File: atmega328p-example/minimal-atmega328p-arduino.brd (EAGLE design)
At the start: 67.3 x 33 mm, 19 parts, among them J1 3x2 M, J4 POWER_JACK, U1 NCP1117ST50T3G, U4 ATMEGA328P-PU, X1 CSTCE16M0V53-R0 16MHZ

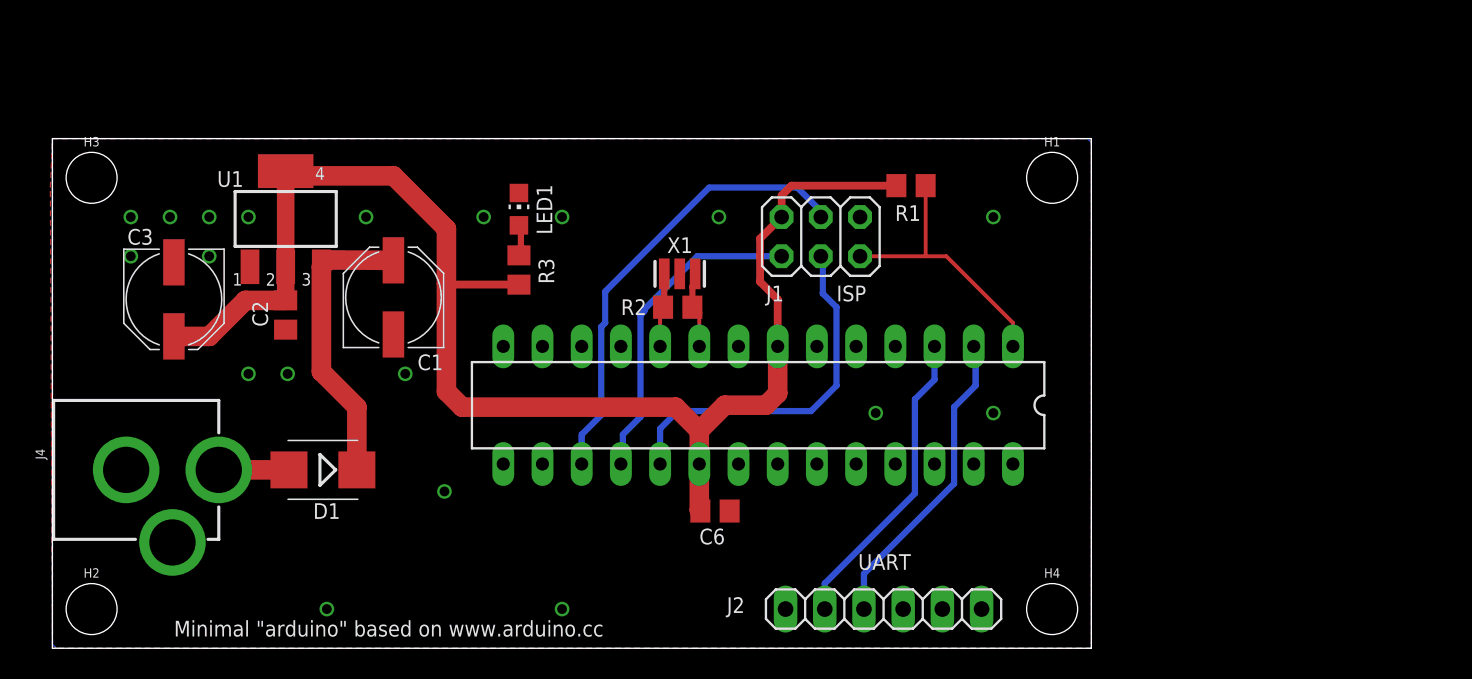
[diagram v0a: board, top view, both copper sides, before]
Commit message: Updated ATMEGA328P schematic and layout to modernish standards. Still needs attributes and BOM.
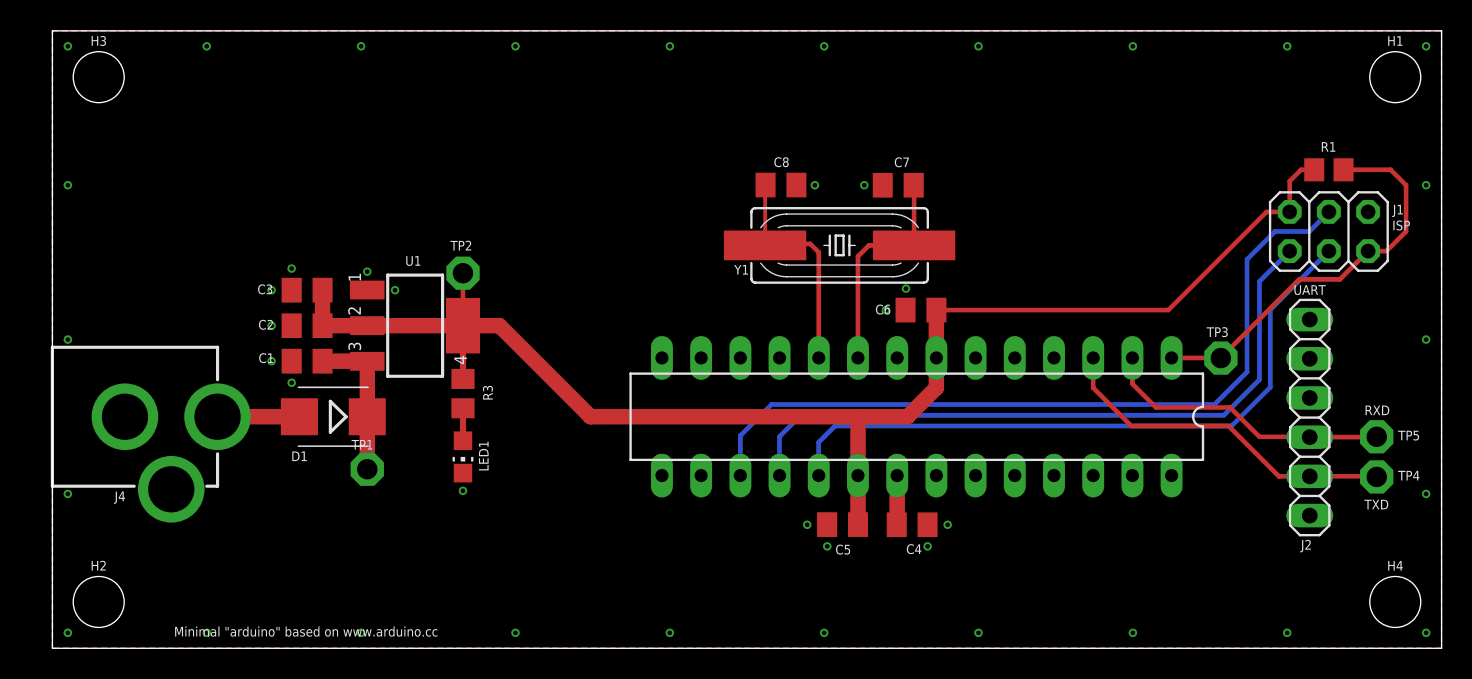
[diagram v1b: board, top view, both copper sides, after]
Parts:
- removed R2: 1M, rcl:R0805
- removed X1: CSTCE16M0V53-R0 16MHZ, SmartPrj:RESONATOR
- added C4, C5: 100n, rcl:C0805K
- added C7, C8: 18p, rcl:C0805K
- added TP1, TP2, TP3, TP4, TP5: TPPAD1-13, testpad:P1-13
- added Y1: 16 MHz, SparkFun-Clocks:HC49UP
- C1, C3: device rcl:PANASONIC_D -> rcl:C0805K
- C2, C6: device rcl:C0805 -> rcl:C0805K
- moved J1 32.9 mm to (82.7, 27.0)
- moved J2 30.3 mm to (81.5, 14.9), turned to 90 degrees
- moved R1 27.1 mm to (82.7, 31.0)
- moved H1 23.2 mm to (87.0, 37.0)
- moved H4 22.2 mm to (87.0, 3.00)
- moved C6 18.6 mm to (56.3, 21.9), turned to 0 degrees
- moved LED1 16.5 mm to (26.6, 12.4), turned to 180 degrees
- moved U1 10.9 mm to (23.5, 20.9), turned to 270 degrees
- moved U4 10.3 mm to (56.0, 15.0)
- moved R3 8.79 mm to (26.6, 16.5), turned to 90 degrees
- moved C3 8.65 mm to (16.5, 23.2), turned to 180 degrees
- moved C1 6.96 mm to (16.5, 18.6), turned to 180 degrees
- moved H3 6.54 mm to (3.00, 37.0)
- moved D1 3.51 mm to (18.2, 15.0)
- moved J4 3.44 mm to (-3.00, 15.0)
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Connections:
- removed net RESET: J1.5, R1.1, U4.1
- new net !RESET: J1.5, R1.1, TP3.TP, U4.1
- new net N$1: C4.2, U4.21
- net +5V: now also C3.1, C5.2, TP2.TP; no longer C3.+
- net GND: now also C1.2, C3.2, C4.1, C5.1, C7.2, C8.2; no longer C1.-, C3.-, X1.2
- net RXD: now also TP5.TP
- net TXD: now also TP4.TP
- net VIN: now also C1.1, TP1.TP; no longer C1.+
- net XTAL1: now also C7.1, Y1.1; no longer R2.1, X1.3
- net XTAL2: now also C8.1, Y1.2; no longer R2.2, X1.1
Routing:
- net !RESET: track 0.00 -> 26.1 mm
- net MISO: track 21.0 -> 44.3 mm
- net MOSI: track 29.6 -> 51.0 mm
- net SCK: track 23.7 -> 43.3 mm
- net RESET: track 17.8 -> 0.00 mm
- net XTAL2: track 4.87 -> 14.5 mm
- net VIN: track 19.0 -> 9.90 mm
- net XTAL1: track 6.34 -> 14.4 mm
- net N$1: track 0.00 -> 3.20 mm
- net TXD: track 20.6 -> 22.7 mm
- net RXD: track 20.3 -> 18.9 mm
- net PWRIN: track 4.55 -> 5.30 mm
- net +5V: track 94.2 -> 93.6 mm
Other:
- board size 67.3 x 33 mm -> 90 x 40 mm
- board text added: "RXD"
- board text added: "TXD"

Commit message: Finished ATMega328P example board.
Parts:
- C1, C3: value 47u -> 10u
- J2: value (none) -> 1x6 M
